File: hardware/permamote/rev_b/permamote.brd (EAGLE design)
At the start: 79.4 x 89.5 mm, 131 parts, among them J1 TC2030-JLINK-L, J2 M10X2, J3 M04X2, Q1 PMDXB950UPEL, Q10 CSD22206W, Q11 CSD22206W, Q2 PMDXB950UPEL, Q3 PMDXB950UPEL, Q4 PMDXB950UPEL, Q5 PMDXB950UPEL, Q6 PMDXB950UPEL, Q7 CSD22206W, Q8 CSD22206W, Q9 CSD22206W, U1 AB1815-T3, U10 NRF52840, U11 SI7021-A20-GM1, U2 BQ25505, U3 EKMB1101111, U4 ISL29125, U5 LIS2DW12, U6 MAX17222, U7 MAX44009, U8 MS5637-02BA03, U9 NRF51822QF, X1 32MHz, X2 ABS05-32.768KHZ-9-T, X3 32.768kHz, X4 ABS07-32.768KHZ-7-T, X5 16MHz

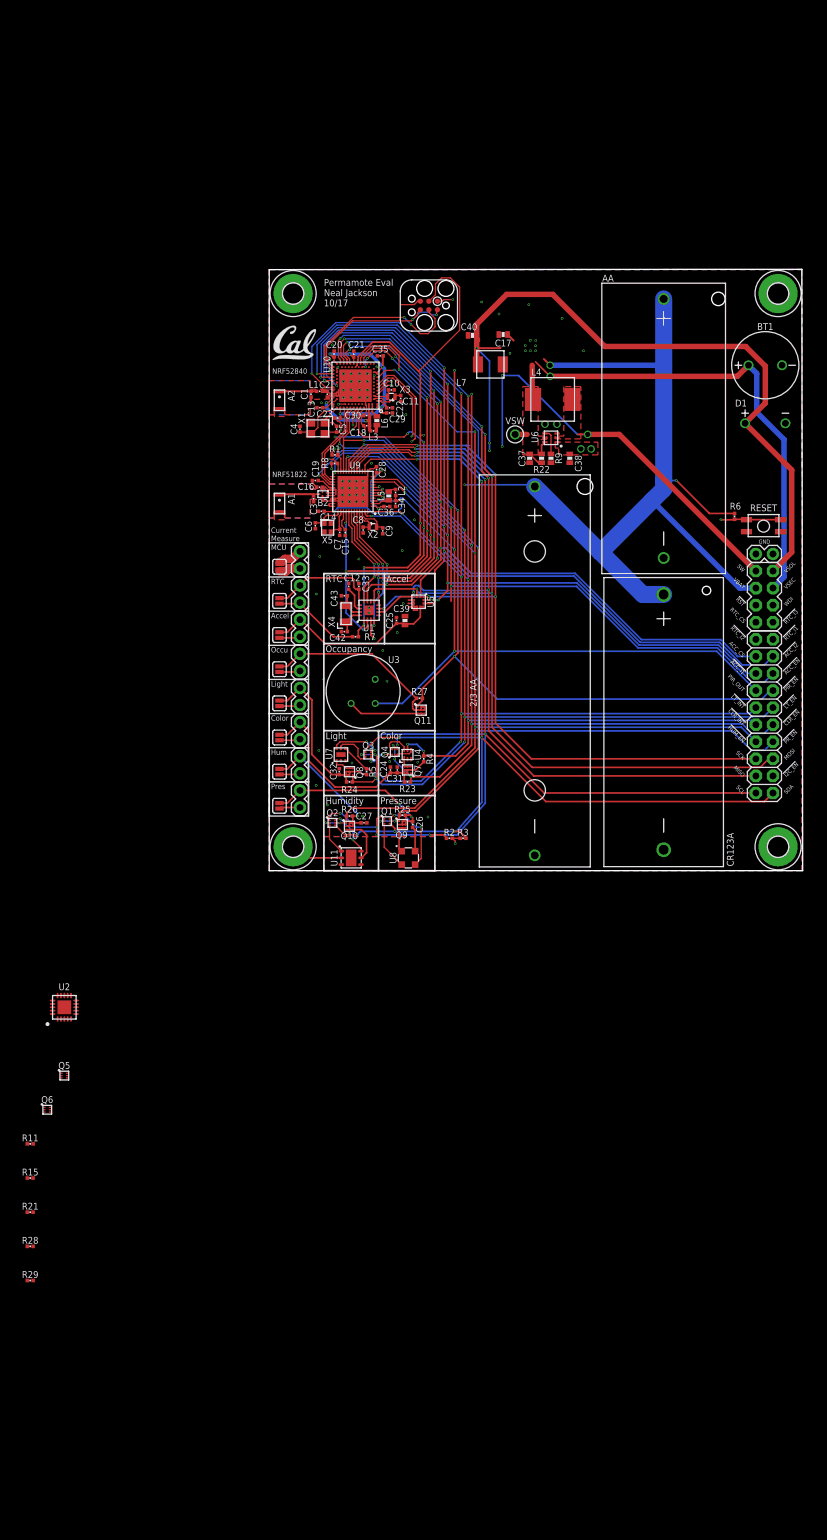
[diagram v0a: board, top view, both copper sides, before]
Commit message: fixed bq dividers, changed inductor
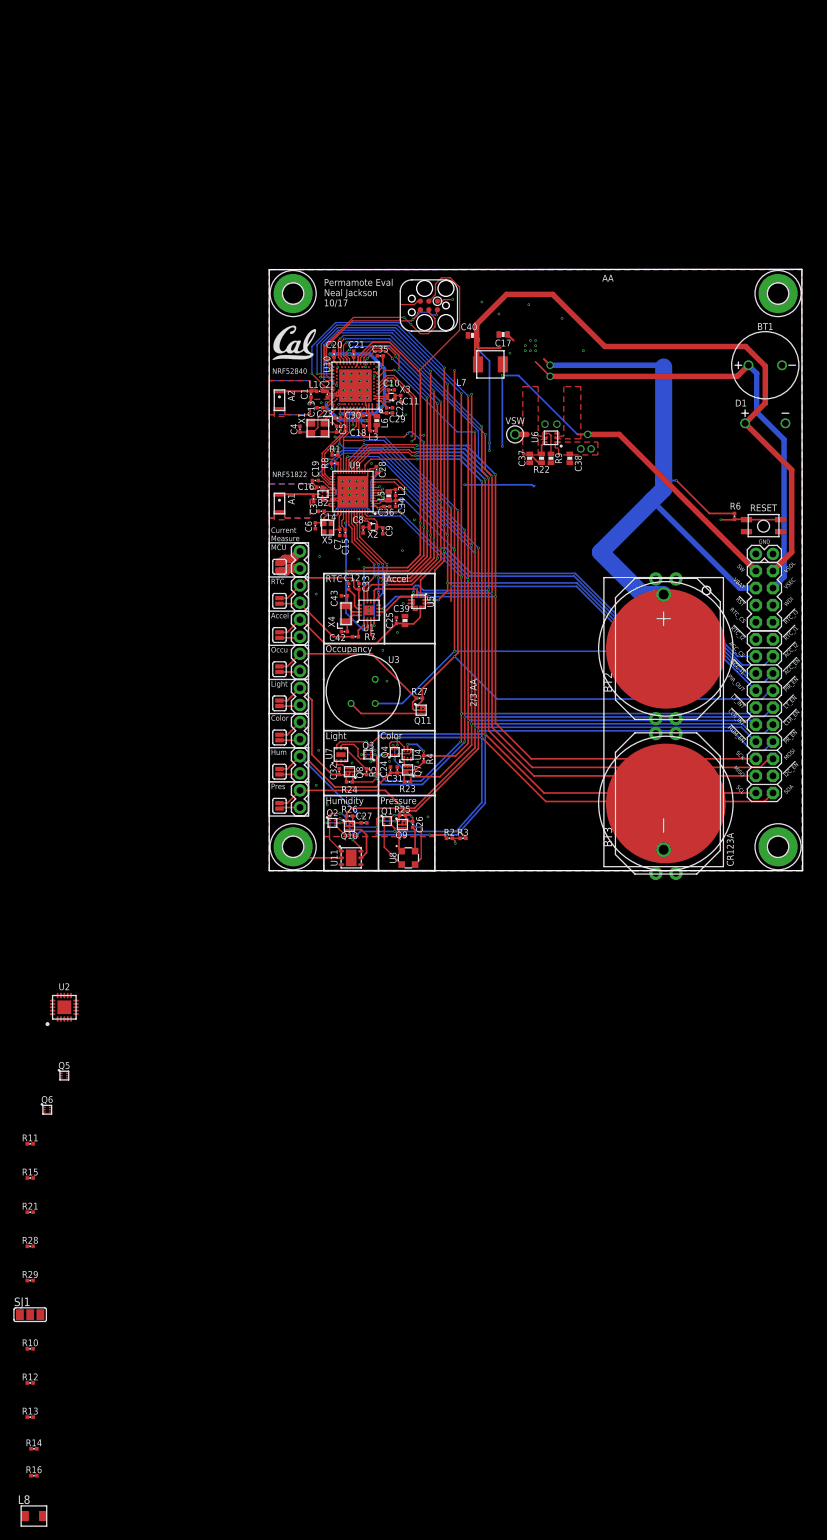
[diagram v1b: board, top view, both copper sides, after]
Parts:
- removed L4: 1uH, passives:IHL-2525CZ
- added L8: 1uH, passives:IHL-1212BZ-11
- added R10: 6.04k, passives:0402_RES
- added R12: 8.87M, passives:0402_RES
- added R13: 4.22M, passives:0402_RES
- added R14: 7.32M, passives:0402_RES
- added R16: 5.62M, passives:0402_RES
- added SJ1: (no value), jumper:SJ_2
- BT2: value BAT_PACK2/3AA -> BAT-HLD-20XX-THRU; device batteries:6S-2-3A -> batteries:BAT-HLD-20XX-THRU
- BT3: value BAT_PACKAA -> BAT-HLD-20XX-THRU; device batteries:BHAA-3 -> batteries:BAT-HLD-20XX-THRU
- R21: value 1.13M -> 6.04k
- R28: value 5M -> 6.19M
- moved BT2 32.8 mm to (59.0, 33.0)
- moved BT3 27.7 mm to (59.0, 10.0)
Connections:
- new net N$1: R11.2, R21.2, SJ1.3
- new net N$16: R10.2, R14.2, SJ1.1
- net GND: now also BT2.GND, BT3.GND, R13.1, R16.1; no longer BT2.-, BT3.-
- net N$18: now also R14.1, R16.2
- net N$32: now also SJ1.2; no longer R11.2, R21.2
- net N$57: now also R12.1, R13.2
- net N$58: now also R10.1, R12.2
- net SW: now also L8.P$2; no longer L4.P$2
- net VBAT: now also BT2.+1, BT2.+2, BT2.+3, BT2.+4, BT3.+1, BT3.+2, BT3.+3, BT3.+4; no longer BT2.+, BT3.+
- net VSW: now also L8.P$1; no longer L4.P$1
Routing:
- net VBAT: track 243.9 -> 219.8 mm
- net VSW: track 9.31 -> 4.17 mm

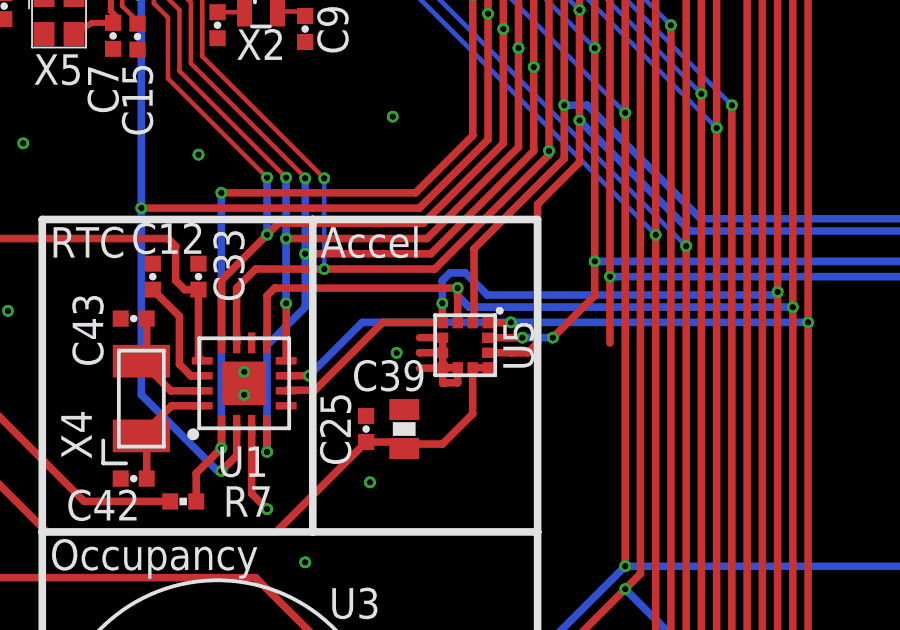
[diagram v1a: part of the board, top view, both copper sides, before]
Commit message: Fix miso/mosi switch
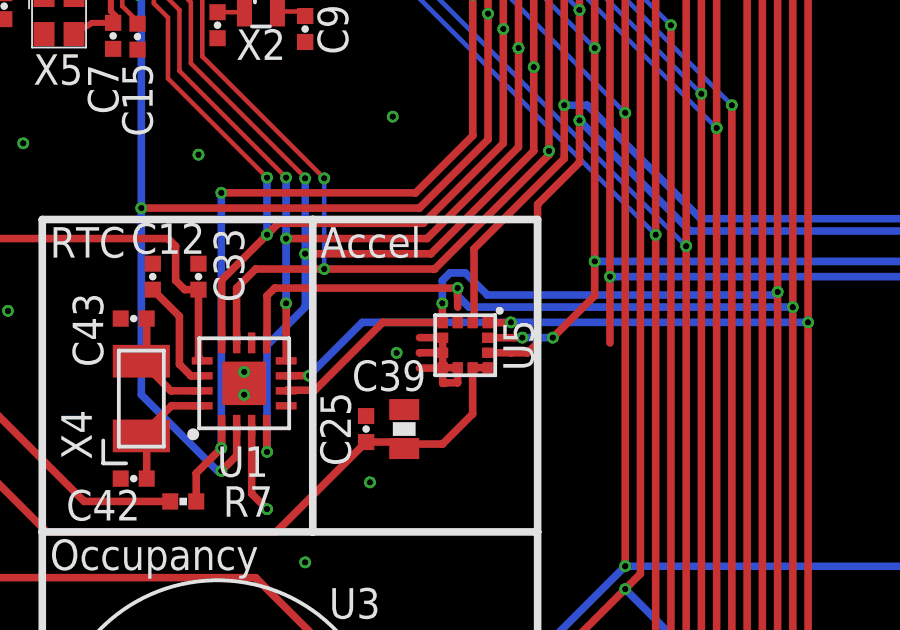
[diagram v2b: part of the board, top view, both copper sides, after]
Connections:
- net MISO: now also U5.3; no longer U5.4
- net MOSI: now also U5.4; no longer U5.3
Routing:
- net MOSI: track 165.1 -> 164.5 mm
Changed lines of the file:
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@@
 <?xml version="1.0" encoding="utf-8"?>
 <!DOCTYPE eagle SYSTEM "eagle.dtd">
-<eagle version="8.4.1">
+<eagle version="8.4.2">
 <drawing>
 <settings>
@@
 <signal name="MISO">
 <contactref element="U1" pad="6"/>
-<contactref element="U5" pad="4"/>
 <contactref element="U10" pad="AD22"/>
 <wire x1="10.577" y1="75.402" x2="10.577" y2="76.053" width="0.1524" layer="1"/>
@@
 <via x="21.463" y="41.402" extent="1-16" drill="0.2032"/>
 <wire x1="21.463" y1="40.767" x2="21.463" y2="41.402" width="0.254" layer="1"/>
-<wire x1="21.463" y1="40.767" x2="21.475" y2="40.755" width="0.254" layer="1"/>
 <wire x1="19.4785" y1="40.767" x2="21.463" y2="40.767" width="0.254" layer="1"/>
 <wire x1="17.2179" y1="38.5064" x2="19.4785" y2="40.767" width="0.254" layer="1"/>
@@
 <wire x1="31.623" y1="66.04" x2="31.623" y2="59.436" width="0.254" layer="1"/>
 <wire x1="31.623" y1="59.436" x2="32.639" y2="58.42" width="0.254" layer="1"/>
+<contactref element="U5" pad="3"/>
+<wire x1="21.463" y1="40.767" x2="21.975" y2="40.755" width="0" layer="19" extent="1-1"/>
 </signal>
 <signal name="MOSI">
 <contactref element="U1" pad="9"/>
-<contactref element="U5" pad="3"/>
 <contactref element="U10" pad="AD20"/>
 <wire x1="11.077" y1="76.061" x2="11.077" y2="75.402" width="0.1524" layer="1"/>
@@
 <via x="33.147" y="41.275" extent="1-16" drill="0.2032"/>
 <wire x1="33.147" y1="58.674" x2="33.147" y2="41.275" width="0.254" layer="1"/>
-<wire x1="21.975" y1="40.755" x2="21.975" y2="41.271" width="0.254" layer="1"/>
 <wire x1="21.971" y1="41.91" x2="21.975" y2="41.271" width="0.254" layer="1"/>
 <via x="21.971" y="41.91" extent="1-16" drill="0.2032"/>
@@
 <wire x1="32.131" y1="64.897" x2="32.131" y2="59.69" width="0.254" layer="1"/>
 <wire x1="32.131" y1="59.69" x2="33.147" y2="58.674" width="0.254" layer="1"/>
+<contactref element="U5" pad="4"/>
+<wire x1="21.975" y1="41.271" x2="21.475" y2="40.755" width="0" layer="19" extent="1-1"/>
 </signal>
 <signal name="!RTC_EXTR">

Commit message: WIP rev_b
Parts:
- removed A1: ANT3216A063R2400A, chips:ANT3216A063R2400A
- removed B2: BAL-NRF01D3, chips:BAL-NRF01D3
- removed C14, C15: 1nF, passives:0402_CAP
- removed C16: 2.2nF, passives:0402_CAP
- removed C19: 47nF, passives:0402_CAP
- removed C28: 0.1uF, passives:0402_CAP
- removed C3: 0.8pF, passives:0402_CAP
- removed C34: 1uF, passives:0402_CAP
- removed C36: 4.7uF, passives:0402_CAP
- removed C6, C7, C8, C9: 12pF, passives:0402_CAP
- removed H1, H2, H3, H4: MOUNT-PAD-ROUND3.0, holes:3,0-PAD
- removed JP1, JP2, JP3, JP4, JP5, JP6, JP7, JP8: (no value), SparkFun-Passives:SJ_2S
- removed JP10, JP11, JP12, JP13, JP14, JP15, JP16, JP9: (no value), SparkFun-Connectors:1X02
- removed L2: 15nH, passives:0402_CAP
- removed L5: 10uH, passives:0603_CAP
- removed Q11, Q9: CSD22206W, fets:DSBGA
- removed R8: 12kΩ, passives:0402_RES
- removed TP10: TEST_POINT_0.040IN, headers:TESTPOINT_0.040IN
- removed U9: NRF51822QF, chips:QFN-48-6MM
- removed X2: ABS05-32.768KHZ-9-T, crystals:ABS05
- removed X5: 16MHz, crystals:TXC-8Y
- added C41: 0.1uF, passives:0402_CAP
- added J5: MICRO_USB_B_HIROSE_ZX62R-B-5P, connector:USB_MICRO_B-HIROSE-ZX62R-B-5P
- added U12: FT232RQ, ftdichip:QFN32
- J1: value TC2030-JLINK-L -> TC2030-JLINK-NL; device connector:TC2030-IDC -> connector:TC2030-IDC-NL
- Q10, Q7, Q8: value CSD22206W -> PMDXB950UPEL; device fets:DSBGA -> fets:XDFN-6
- R1: value 150Ω -> 10kΩ
- moved R16 161.2 mm to (5.84, 65.9), turned to 180 degrees
- moved R14 158.4 mm to (5.84, 67.1)
- moved R13 153.5 mm to (7.87, 65.9)
- moved L8 151.3 mm to (34.0, 38.6)
- moved R12 149.7 mm to (7.87, 67.1), turned to 180 degrees
- moved R10 145.5 mm to (6.99, 68.1), turned to 180 degrees
- moved SJ1 137.3 mm to (11.3, 63.0)
- moved R29 134.8 mm to (9.91, 65.9), turned to 180 degrees
- moved R28 131.1 mm to (9.91, 67.1)
- moved R21 127.6 mm to (10.8, 68.1)
- moved R15 121.3 mm to (11.9, 65.9)
- moved R11 117.7 mm to (11.9, 67.1), turned to 180 degrees
- moved Q6 116.2 mm to (14.6, 70.5)
- moved Q5 108.6 mm to (1.02, 73.4)
- moved R1 108.2 mm to (-7.00, -45.0)
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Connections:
- removed net AVDD1: C14.1, C34.1, L2.1, U9.35, U9.36
- removed net DCC1: L5.2, U9.2
- removed net N$15: C25.1, C39.1, JP1.1, JP11.1, U5.10, U5.9
- removed net N$19: C26.1, JP15.1, JP4.1, Q9.A2, Q9.A3, Q9.B1, Q9.B2, Q9.B3, R25.2
- removed net N$24: JP14.1, JP8.1, Q11.A2, Q11.A3, Q11.B1, Q11.B2, Q11.B3, R27.2
- removed net N$33: C24.1, C31.1, JP12.1, JP2.1, Q7.A2, Q7.A3, Q7.B1, Q7.B2, Q7.B3, R23.2, R4.2
- removed net N$36: C27.1, JP16.1, JP5.1, Q10.A2, Q10.A3, Q10.B1, Q10.B2, Q10.B3, R26.2
- removed net N$37: C32.1, JP13.1, JP3.1, Q8.A2, Q8.A3, Q8.B1, Q8.B2, Q8.B3, R24.2, R5.2
- removed net N$42: C33.1, JP10.1, JP6.1, U1.13
- removed net N$60: B2.ANT1, U9.31
- removed net N$61: B2.ANT2, U9.32
- removed net N$62: A1.S1, B2.SE, C3.1
- removed net N$63: L2.2, L5.1
- removed net N$64: C6.1, U9.37, X5.1
- removed net N$65: C7.1, U9.38, X5.3
- removed net N$66: C15.1, U9.39
- removed net N$67: C19.1, U9.29
- removed net NRF_A2: C9.1, U9.46, X2.B
- removed net NRF_A3: C8.1, U9.45, X2.A
- removed net VCC_JUMP: C20.1, C21.1, C23.1, C28.1, C29.1, C35.1, C36.1, JP7.1, JP9.1, U10.A22, U10.AD14, U10.AD23, U10.B1, U10.W1, U10.Y2, U9.1, U9.12
- removed net VDD_PA1: B2.VCC, C16.1, U9.30
- new net D+: J5.3, U12.14
- new net D-: J5.2, U12.15
- new net DBG_RX: U12.30
- new net DBG_TX: U12.2
- new net N$13: C41.1, U12.16
- new net USB_5V: J5.1, U12.19
- net !ACC_EN: no longer U10.A14, U9.22
- net !CLR_EN: now also Q7.2; no longer Q7.A1, U9.25
- net !CLR_INT: no longer U9.48
- net !HUM_EN: now also Q8.5; no longer Q10.A1, U9.21
- net !LT_EN: now also Q7.5; no longer Q8.A1, U9.26
- net !LT_INT: no longer U9.47
- net !PIR_EN: now also Q10.2; no longer Q11.A1, U9.27
- net !PR_EN: now also Q8.2; no longer Q9.A1, U9.28
- net !RST: now also U12.18; no longer R1.1
- net !RTC_IRQ1: no longer U9.44
- net !RTC_IRQ2: no longer U9.43
- net !RTC_IRQ3: no longer U9.42
- net ACC_CS: no longer U9.20
- net ACC_INT1: no longer U9.10
- net ACC_INT2: no longer U9.11
- net GND: now also C41.2, J5.5, U12.17, U12.20, U12.24, U12.26, U12.4; no longer A1.S2, B2.GND, C14.2, C15.2, C16.2, C19.2, C28.2, C3.2, C34.2, C36.2, C6.2, C7.2, C8.2, C9.2, H1.B3,0, H2.B3,0, H3.B3,0, H4.B3,0, R8.2, U9.13, U9.33, U9.34, U9.GND
- net MISO: no longer U9.17
- net MOSI: no longer U9.18
- net N$20: now also Q7.3; no longer Q8.C1, Q8.C2, Q8.C3
- net N$21: now also Q8.6; no longer Q9.C1, Q9.C2, Q9.C3
- net N$22: now also Q8.3; no longer Q10.C1, Q10.C2, Q10.C3
- net N$23: now also Q10.6; no longer Q11.C1, Q11.C2, Q11.C3
- net N$31: now also Q7.6; no longer Q7.C1, Q7.C2, Q7.C3
- net PIR_OUT: no longer U9.3
- net RTC_CS: no longer U9.41
- net SCK: no longer U9.19
- net SCL: no longer U9.16
- net SDA: no longer U9.14
- net SW: no longer U9.8
- net SWDCLK: no longer R8.1, U9.24
- net SWDIO: no longer J1.6, R1.2, U9.23
- net VBAT: now also U1.5; no longer JP10.2, JP6.2, R6.2, R7.2, U9.6
- net VCC: now also C20.1, C21.1, C23.1, C24.1, C25.1, C26.1, C27.1, C29.1, C31.1, C32.1, C33.1, C35.1, C39.1, Q10.1, Q7.1, Q7.4, Q8.1, Q8.4, R1.2, R23.2, R24.2, R25.2, R26.2, R27.2, R4.2, R5.2, R6.2, R7.2, U1.13, U10.A22, U10.AD14, U10.AD23, U10.B1, U10.W1, U10.Y2, U12.1, U5.10, U5.9; no longer JP1.2, JP11.2, JP12.2, JP13.2, JP14.2, JP15.2, JP16.2, JP2.2, JP3.2, JP4.2, JP5.2, JP7.2, JP8.2, JP9.2
- net VSEC: no longer U9.5
- net VSOL: no longer U9.7
- net VSW: no longer TP10.TESTPOINT
- net WDI: now also R1.1; no longer U9.40
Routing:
- net VBAT: track 219.8 -> 0.00 mm, vias 5 -> 0
- net SCL: track 187.9 -> 3.34 mm, vias 10 -> 2
- net SDA: track 181.7 -> 1.61 mm, vias 9 -> 2
- net !LT_INT: track 169.0 -> 2.93 mm, vias 7 -> 1
- net !HUM_EN: track 164.7 -> 0.00 mm, vias 7 -> 0
- net MOSI: track 164.5 -> 0.00 mm, vias 6 -> 0
- net MISO: track 161.8 -> 0.00 mm, vias 6 -> 0
- net !RST: track 160.4 -> 0.00 mm, vias 5 -> 0
- net !CLR_EN: track 162.7 -> 5.91 mm, vias 8 -> 3
- net SCK: track 155.9 -> 0.00 mm, vias 6 -> 0
- net VSOL: track 155.2 -> 0.00 mm, vias 5 -> 0
- net !CLR_INT: track 160.5 -> 6.21 mm, vias 7 -> 2
- net !PR_EN: track 144.1 -> 0.00 mm, vias 6 -> 0
- net ACC_INT2: track 139.1 -> 0.00 mm, vias 5 -> 0
- net PIR_OUT: track 138.5 -> 0.00 mm, vias 5 -> 0
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- added copper zone on layer 1, net N$10
- added copper zone on layer 15, net N$10
- added copper zone on layer 16, net N$10
- added copper zone on layer 2, net N$10
- removed copper zone on layer 15, net N$38
- removed copper zone on layer 16, net N$38
- removed copper zone on layer 2, net N$38
- removed copper zone on layer 1, net N$43
- removed copper zone on layer 15, net N$43
- removed copper zone on layer 16, net N$43
- removed copper zone on layer 2, net N$43
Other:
- board size 79.4 x 89.5 mm -> 25 x 54.1 mm
- board text removed: "2/3 AA"
- board text removed: "AA"
- board text removed: "CR123A"
- board text removed: "Current Measure"
- board text removed: "Hum"
- board text removed: "MCU"
- board text removed: "NRF51822"
- board text removed: "NRF52840"
- board text removed: "Occu"
- board text removed: "Pres"
